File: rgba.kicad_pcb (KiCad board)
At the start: 4 copper layers, 40 x 22 mm, 74 parts, among them J1 CHARGE CONN, J11 Screw 1, J12 Screw 1, J2 BATT CONN, J3 UART_GND, J4 R SPK OUT, J5 L SPK OUT, J6 UART_TX, J7 UART_VBUS, J8 UART_RX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

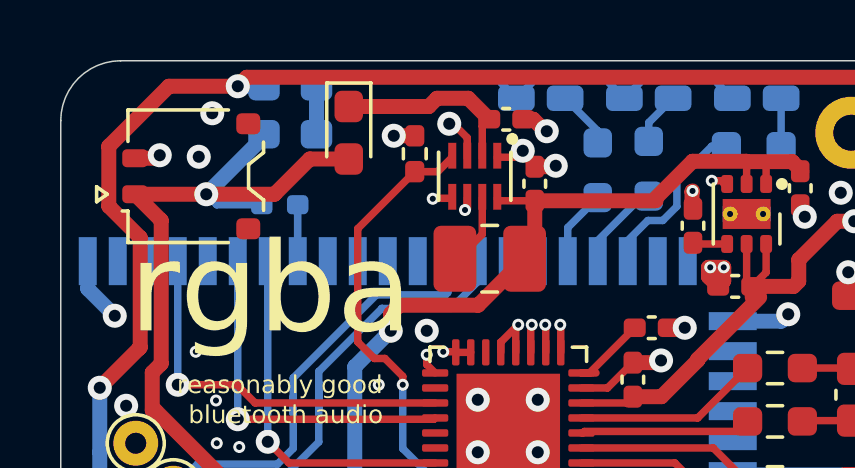
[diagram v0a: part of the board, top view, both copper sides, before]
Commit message: remove TPS62849 enable pin pulldown resistor because it has an internal pulldown resistor
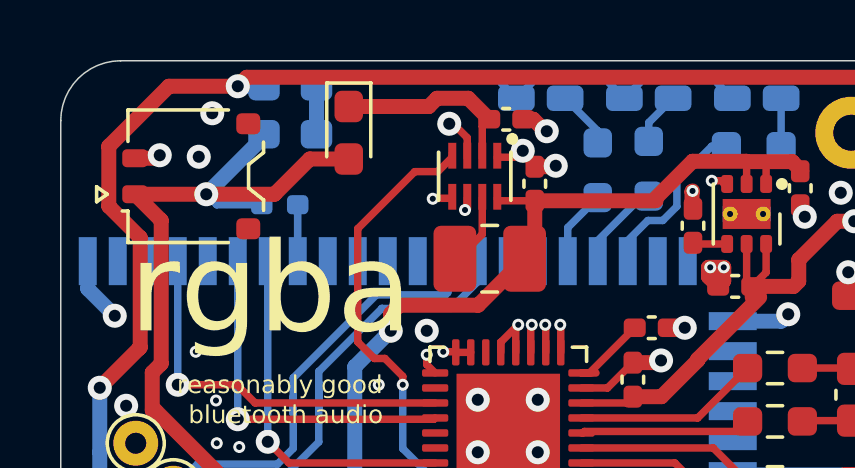
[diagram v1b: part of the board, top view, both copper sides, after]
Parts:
- removed R30: 100K, Resistor_SMD:R_0402_1005Metric_Pad0.72x0.64mm_HandSolder
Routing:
- net GND: track 73.8 -> 73.1 mm, vias 76 -> 75
